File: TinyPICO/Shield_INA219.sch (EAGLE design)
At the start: 11 parts, among them J1 3.5mm, U1 INA219BIDCNT

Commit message: Prettied up the boards a little
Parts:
- added R5+, R5-: (no value), wirepad:1,6/0,9
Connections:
- net VIN1+: now also R5+.P
- net VIN1-: now also R5-.P
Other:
- moved on the sheet: R5
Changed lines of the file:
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@@
 <part name="JP2" library="microbuilder" deviceset="HEADER-1X2" device="ROUND"/>
 <part name="R6" library="microbuilder" deviceset="RESISTOR_4PACK" device="" value="10K"/>
+<part name="R5+" library="wirepad" library_urn="urn:adsk.eagle:library:412" deviceset="1,6/0,9" device="" package3d_urn="urn:adsk.eagle:package:30840/1"/>
+<part name="R5-" library="wirepad" library_urn="urn:adsk.eagle:library:412" deviceset="1,6/0,9" device="" package3d_urn="urn:adsk.eagle:package:30840/1"/>
 </parts>
 <sheets>
@@
 <attribute name="VALUE" x="51.816" y="134.62" size="1.27" layer="96"/>
 </instance>
-<instance part="R5" gate="G$1" x="119.38" y="134.62" smashed="yes" rot="R90">
-<attribute name="NAME" x="116.84" y="134.62" size="1.27" layer="95" font="vector" rot="R90" align="center"/>
-<attribute name="VALUE" x="119.38" y="134.62" size="1.016" layer="96" font="vector" ratio="15" rot="R90" align="center"/>
+<instance part="R5" gate="G$1" x="114.3" y="134.62" smashed="yes" rot="R90">
+<attribute name="NAME" x="111.76" y="134.62" size="1.27" layer="95" font="vector" rot="R90" align="center"/>
+<attribute name="VALUE" x="114.3" y="134.62" size="1.016" layer="96" font="vector" ratio="15" rot="R90" align="center"/>
 </instance>
 <instance part="J1" gate="G$1" x="129.54" y="137.16" smashed="yes" rot="MR180">
@@
 <attribute name="NAME" x="58.42" y="121.92" size="1.27" layer="95" font="vector" rot="R270" align="center"/>
 <attribute name="VALUE" x="55.88" y="121.92" size="1.016" layer="96" font="vector" ratio="15" rot="R270" align="center"/>
+</instance>
+<instance part="R5+" gate="1" x="116.84" y="139.7" smashed="yes" rot="R180">
+<attribute name="NAME" x="118.237" y="138.8618" size="1.778" layer="95"/>
+<attribute name="VALUE" x="117.983" y="143.002" size="1.778" layer="96" rot="R180"/>
+</instance>
+<instance part="R5-" gate="1" x="116.84" y="129.54" smashed="yes" rot="R180">
+<attribute name="NAME" x="118.491" y="128.7018" size="1.778" layer="95"/>
+<attribute name="VALUE" x="117.983" y="132.842" size="1.778" layer="96" rot="R180"/>
 </instance>
 </instances>
@@
 <net name="VIN1+" class="0">
 <segment>
-<wire x1="104.14" y1="137.16" x2="114.3" y2="137.16" width="0.1524" layer="91"/>
-<wire x1="114.3" y1="137.16" x2="114.3" y2="142.24" width="0.1524" layer="91"/>
-<wire x1="114.3" y1="142.24" x2="119.38" y2="142.24" width="0.1524" layer="91"/>
-<wire x1="119.38" y1="142.24" x2="119.38" y2="139.7" width="0.1524" layer="91"/>
-<label x="106.68" y="137.16" size="1.778" layer="95"/>
+<wire x1="104.14" y1="137.16" x2="111.76" y2="137.16" width="0.1524" layer="91"/>
+<wire x1="111.76" y1="137.16" x2="111.76" y2="142.24" width="0.1524" layer="91"/>
+<wire x1="111.76" y1="142.24" x2="114.3" y2="142.24" width="0.1524" layer="91"/>
+<wire x1="114.3" y1="142.24" x2="114.3" y2="139.7" width="0.1524" layer="91"/>
+<label x="104.14" y="137.16" size="1.778" layer="95"/>
 <pinref part="U1" gate="G$1" pin="VIN+"/>
 <pinref part="R5" gate="G$1" pin="2"/>
-<junction x="119.38" y="142.24"/>
+<junction x="114.3" y="142.24"/>
 <pinref part="J1" gate="G$1" pin="2"/>
-<wire x1="124.46" y1="142.24" x2="119.38" y2="142.24" width="0.1524" layer="91"/>
+<wire x1="124.46" y1="142.24" x2="114.3" y2="142.24" width="0.1524" layer="91"/>
 <wire x1="124.46" y1="137.16" x2="124.46" y2="142.24" width="0.1524" layer="91"/>
+<pinref part="R5+" gate="1" pin="P"/>
+<junction x="114.3" y="139.7"/>
 </segment>
 <segment>
@@
 <net name="VIN1-" class="0">
 <segment>
-<wire x1="104.14" y1="129.54" x2="114.3" y2="129.54" width="0.1524" layer="91"/>
-<wire x1="114.3" y1="129.54" x2="114.3" y2="124.46" width="0.1524" layer="91"/>
-<wire x1="114.3" y1="124.46" x2="119.38" y2="124.46" width="0.1524" layer="91"/>
-<wire x1="119.38" y1="124.46" x2="119.38" y2="129.54" width="0.1524" layer="91"/>
-<label x="106.68" y="129.54" size="1.778" layer="95"/>
+<wire x1="104.14" y1="129.54" x2="111.76" y2="129.54" width="0.1524" layer="91"/>
+<wire x1="111.76" y1="129.54" x2="111.76" y2="124.46" width="0.1524" layer="91"/>
+<wire x1="111.76" y1="124.46" x2="114.3" y2="124.46" width="0.1524" layer="91"/>
+<wire x1="114.3" y1="124.46" x2="114.3" y2="129.54" width="0.1524" layer="91"/>
+<label x="104.14" y="129.54" size="1.778" layer="95"/>
 <pinref part="U1" gate="G$1" pin="VIN-"/>
 <pinref part="R5" gate="G$1" pin="1"/>
-<junction x="119.38" y="124.46"/>
+<junction x="114.3" y="124.46"/>
 <pinref part="J1" gate="G$1" pin="1"/>
-<wire x1="119.38" y1="124.46" x2="124.46" y2="124.46" width="0.1524" layer="91"/>
+<wire x1="114.3" y1="124.46" x2="124.46" y2="124.46" width="0.1524" layer="91"/>
 <wire x1="124.46" y1="124.46" x2="124.46" y2="134.62" width="0.1524" layer="91"/>
-</segment>
-<segment>
+<pinref part="R5-" gate="1" pin="P"/>
+<junction x="114.3" y="129.54"/>
+</segment>
+<segment>

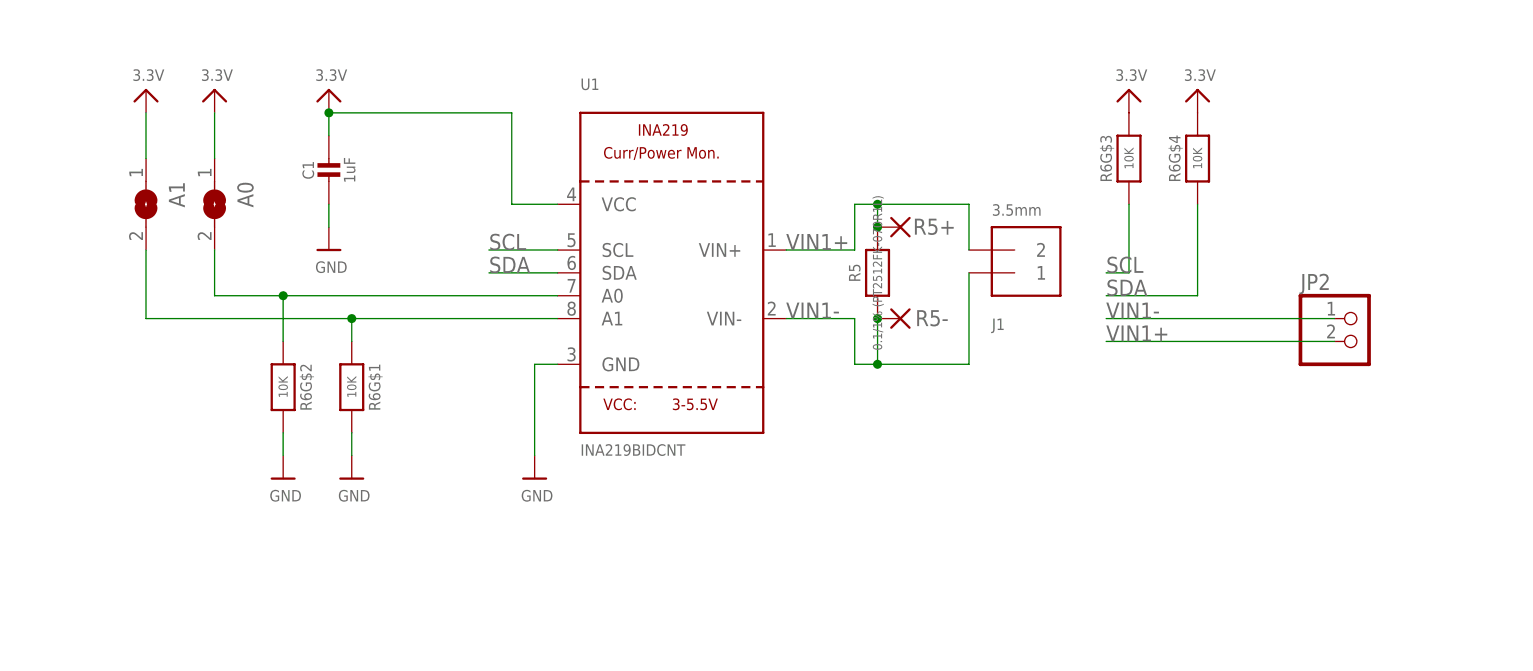
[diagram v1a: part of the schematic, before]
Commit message: TinyPICO Shield Ammeter INA219 v2.1
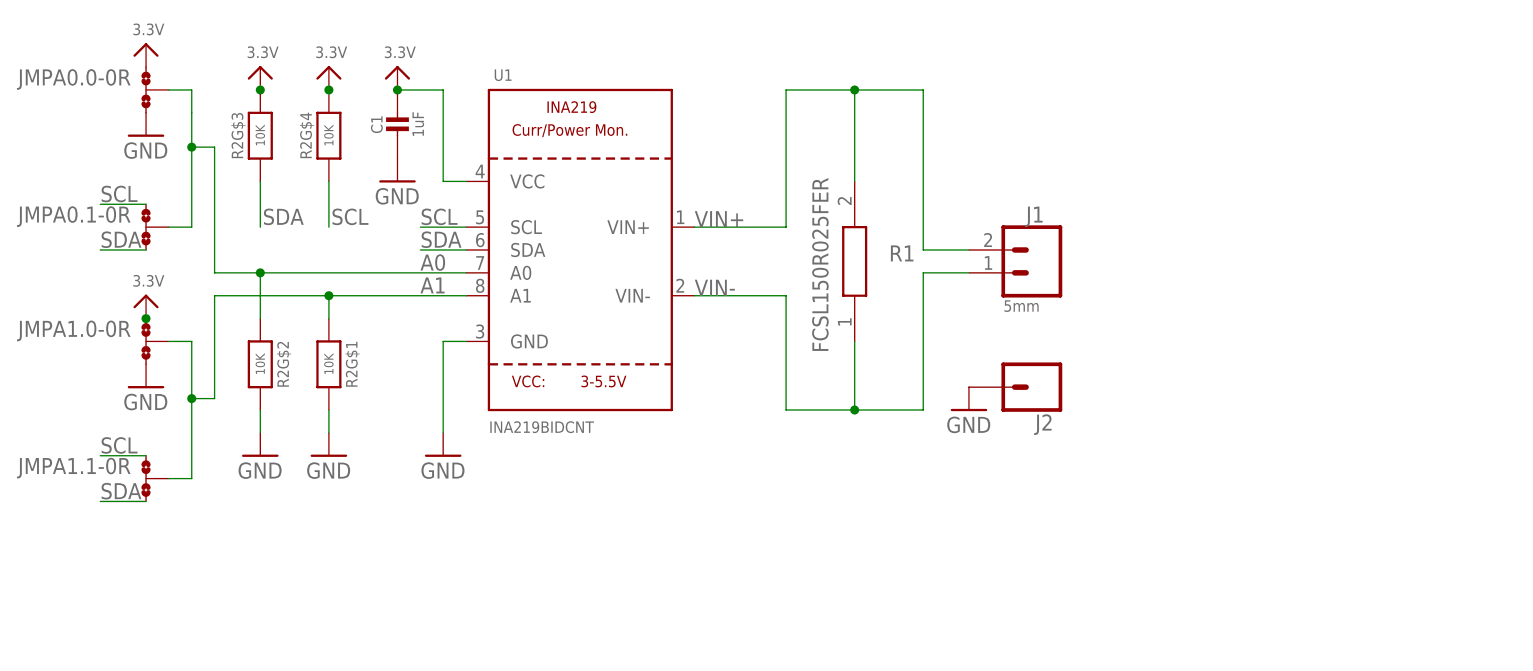
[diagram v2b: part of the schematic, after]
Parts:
- removed A0, A1: (no value), microbuilder:SOLDERJUMPERREFLOW_NOPASTE
- removed JP2: (no value), microbuilder:HEADER-1X2ROUND
- removed R5: 0.1/1% (PT2512FK-070R1L), microbuilder:RESISTOR2512
- removed R5+, R5-: (no value), wirepad:1,6/0,9
- removed R6: 10K, microbuilder:RESISTOR_4PACK
- added J2: (no value), SparkFun-Connectors:CONN_01
- added JMPA0.0, JMPA0.1, JMPA1.0, JMPA1.1: 0R-JUMPD, pv_jump-0r-smd:0R-JUMPD
- added R1: FCSL150R025FER, pv:FCSL150R025FER
- added R2: 10K, microbuilder:RESISTOR_4PACK
- J1: value 3.5mm -> 5mm; device microbuilder:TERMBLOCK_1X2 -> SparkFun-Connectors:CONN_025MM
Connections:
- removed net N$1: A1.2, R6G$1.1, U1.A1
- removed net N$2: A0.2, R6G$2.1, U1.A0
- removed net VIN1+: J1.2, JP2.2, R5+.P, R5.2, U1.VIN+
- removed net VIN1-: J1.1, JP2.1, R5-.P, R5.1, U1.VIN-
- new net A0: JMPA0.0-0R.2, JMPA0.1-0R.2, R2G$2.1, U1.A0
- new net A1: JMPA1.0-0R.2, JMPA1.1-0R.2, R2G$1.1, U1.A1
- new net VIN+: J1.2, R1.2, U1.VIN+
- new net VIN-: J1.1, R1.1, U1.VIN-
- net 3.3V: now also JMPA0.0-0R.1, JMPA1.0-0R.1, R2G$3.2, R2G$4.2; no longer A0.1, A1.1, R6G$3.2, R6G$4.2
- net GND: now also J2.1, JMPA0.0-0R.3, JMPA1.0-0R.3, R2G$1.2, R2G$2.2; no longer R6G$1.2, R6G$2.2
- net SCL: now also JMPA0.1-0R.1, JMPA1.1-0R.1, R2G$4.1; no longer R6G$3.1
- net SDA: now also JMPA0.1-0R.3, JMPA1.1-0R.3, R2G$3.1; no longer R6G$4.1
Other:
- moved on the sheet: C1, U1
